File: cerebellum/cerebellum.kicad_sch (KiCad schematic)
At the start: 18 parts, among them J1 GPIO, SW1 SW_PULLUP, SW2 SW_PULLDOWN, SW3 SW_SPDT, U1 CAT24C256, U2 POLOLU_TB6612_CARRIER, U3 HC-SR04

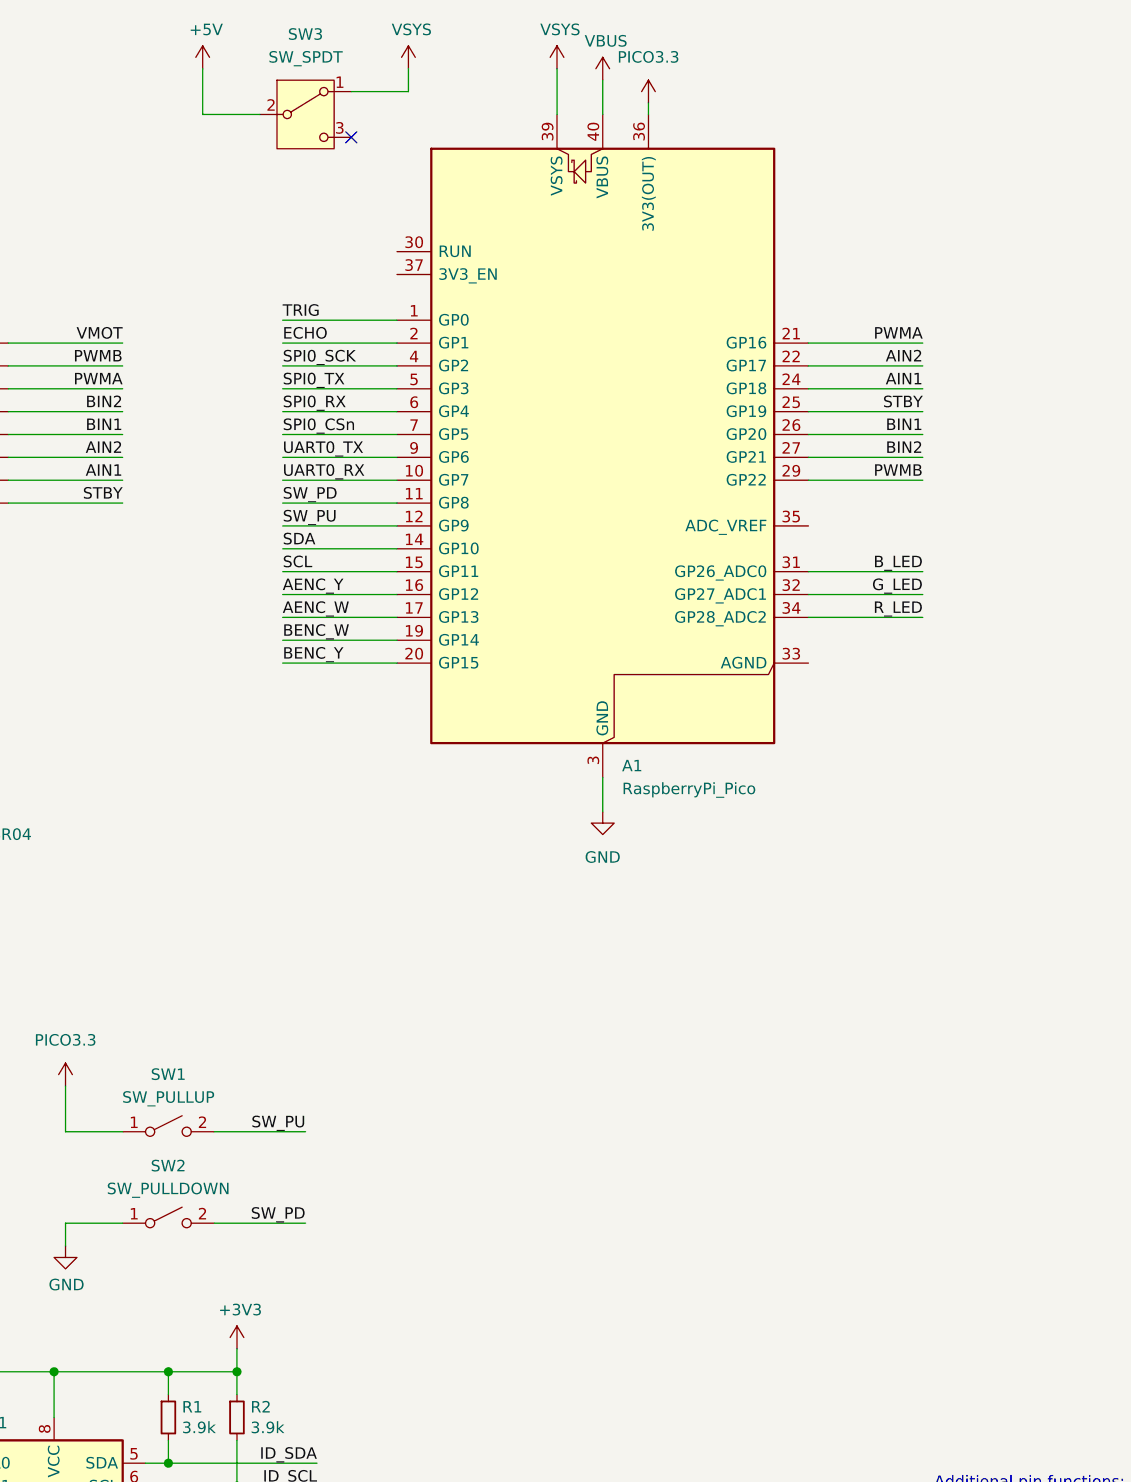
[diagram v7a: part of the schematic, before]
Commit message: update schematic
added motor connectors
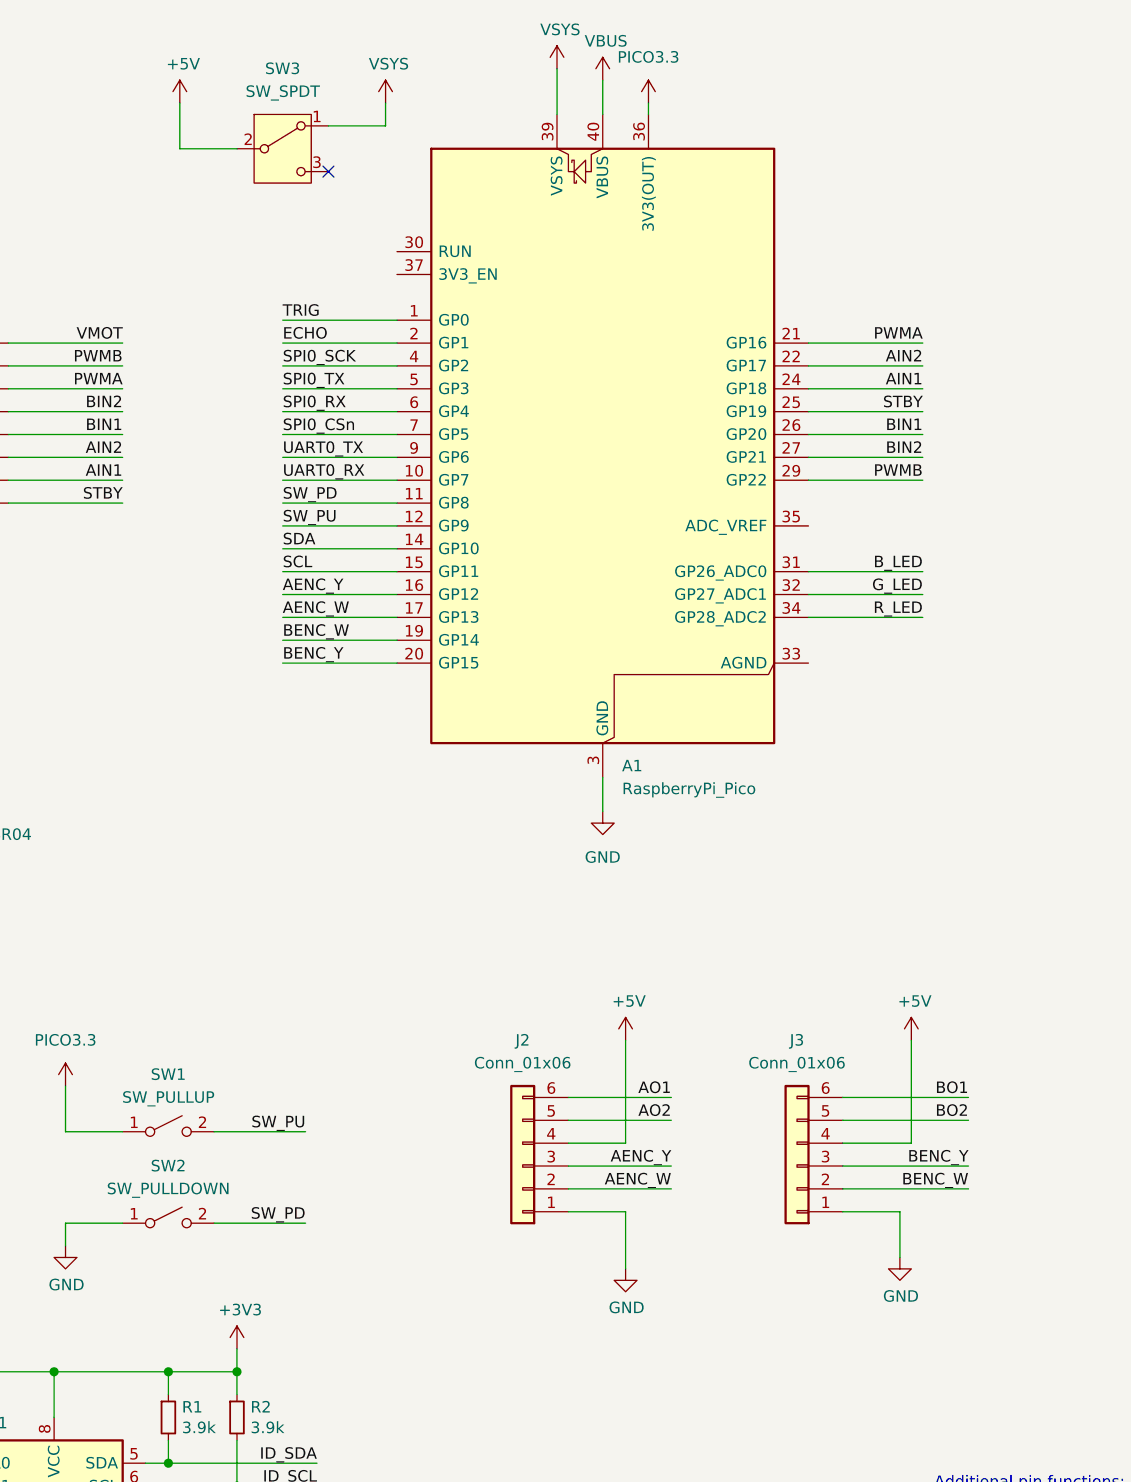
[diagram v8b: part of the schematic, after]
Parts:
- added J2, J3: Conn_01x06, symbol Connector_Generic:Conn_01x06
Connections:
- net +5V: now also J2.4 (Pin_4), J3.4 (Pin_4)
- net AENC_W: now also J2.2 (Pin_2)
- net AENC_Y: now also J2.3 (Pin_3)
- net AO1: now also J2.6 (Pin_6)
- net AO2: now also J2.5 (Pin_5)
- net BENC_W: now also J3.2 (Pin_2)
- net BENC_Y: now also J3.3 (Pin_3)
- net BO1: now also J3.6 (Pin_6)
- net BO2: now also J3.5 (Pin_5)
- net GND: now also J2.1 (Pin_1), J3.1 (Pin_1)
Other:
- moved on the sheet: SW3
